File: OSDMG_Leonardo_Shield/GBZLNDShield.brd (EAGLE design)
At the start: 81.3 x 52.1 mm, 12 parts

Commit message: update
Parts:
- moved B1 31.5 mm to (67.5, 35.1)
- moved JP2 3.96 mm to (32.0, 45.4)
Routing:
- net N$8: track 79.8 -> 47.9 mm, vias 0 -> 3
- net N$10: track 15.0 -> 41.2 mm, vias 0 -> 1
- net N$7: track 47.7 -> 66.6 mm
- net N$3: track 52.2 -> 70.9 mm
- net N$5: track 92.2 -> 108.7 mm, vias 0 -> 1
- net N$12: track 53.7 -> 38.4 mm, vias 0 -> 1
- net N$1: track 62.6 -> 75.8 mm, vias 0 -> 2
- net N$14: track 21.3 -> 31.9 mm, vias 1 -> 2
- net N$2: track 65.6 -> 75.7 mm
- net N$11: track 69.8 -> 79.0 mm, vias 0 -> 2
- net N$6: track 15.6 -> 23.6 mm
- net N$4: track 52.1 -> 57.5 mm, vias 0 -> 1
- net N$15: track 25.3 -> 30.0 mm, vias 0 -> 1
- net N$13: track 50.4 -> 45.9 mm, vias 0 -> 1
- net N$9: track 21.7 -> 20.0 mm
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
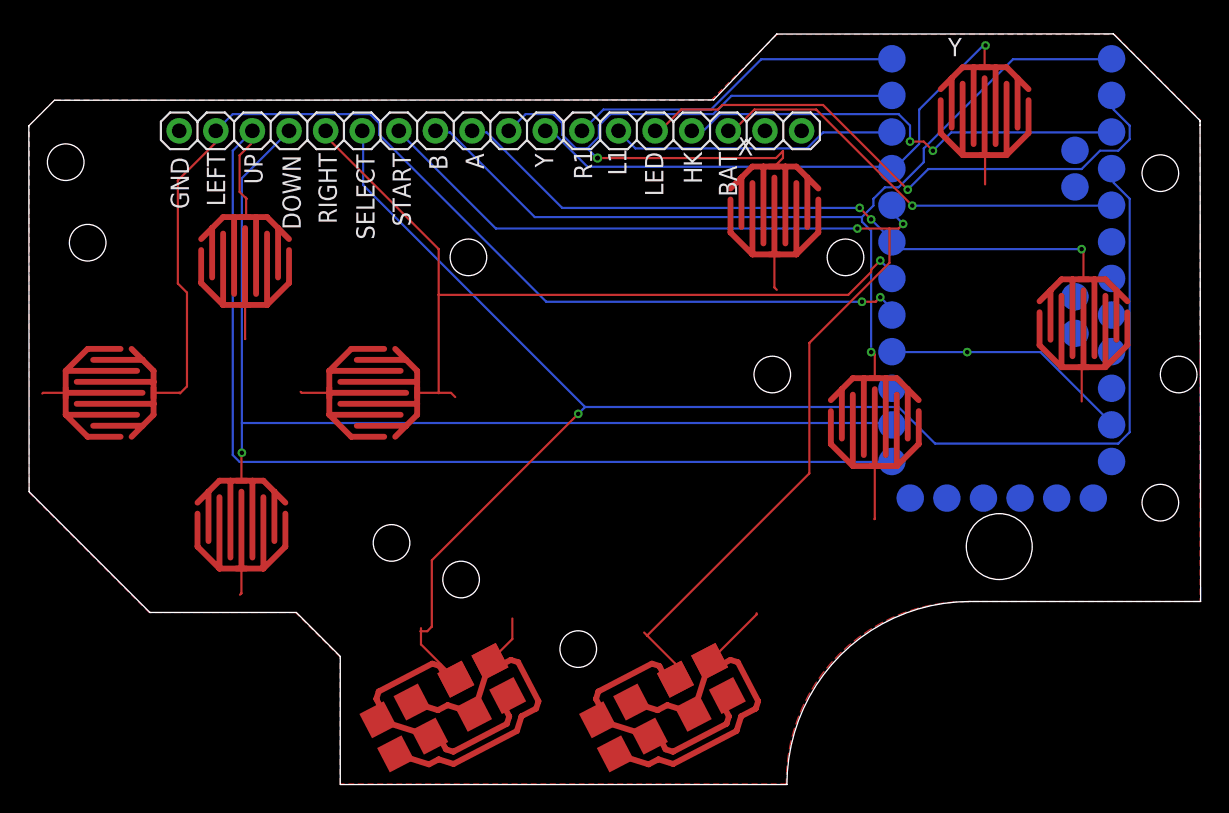
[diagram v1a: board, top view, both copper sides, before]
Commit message: update board
5V and GND Pads and better placement of the leonardo
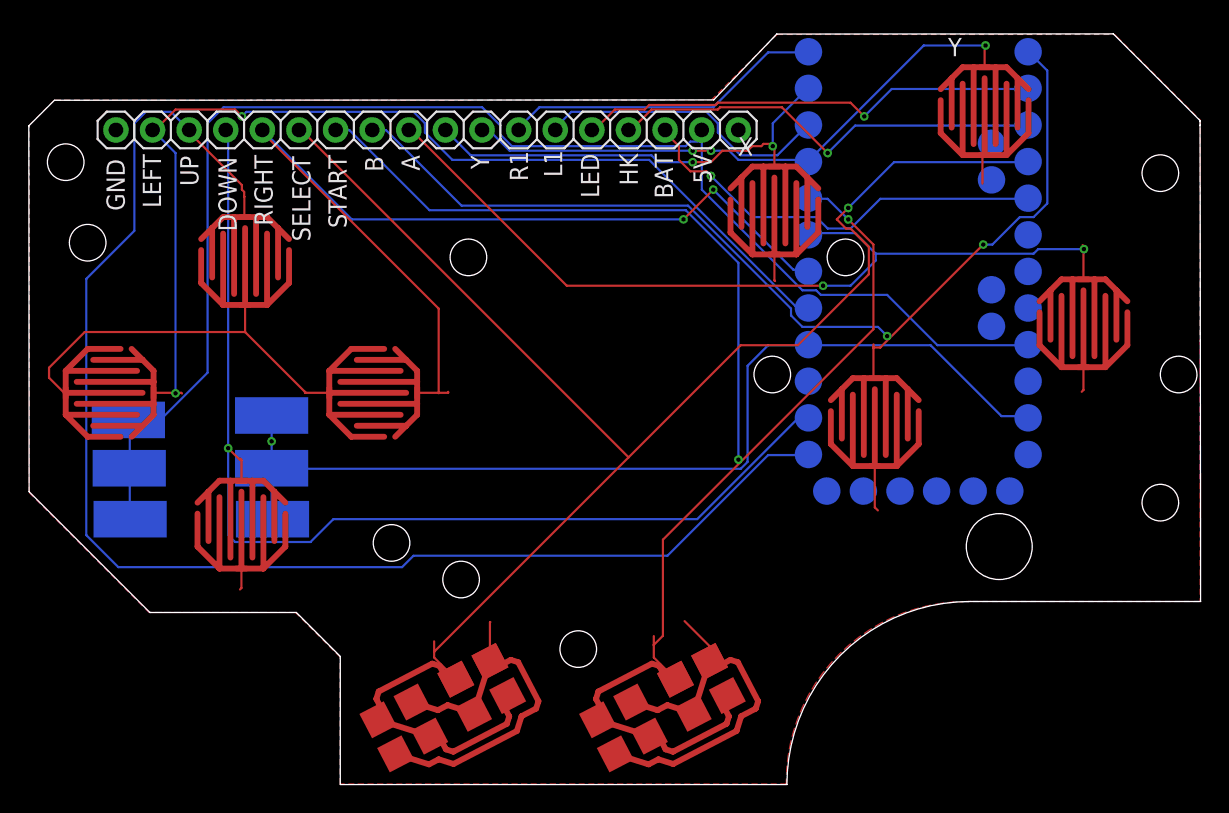
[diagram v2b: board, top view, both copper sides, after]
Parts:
- added PAD1, PAD2, PAD3, PAD4, PAD5, PAD6: (no value), wirepad:SMD2,54-5,08
- moved B1 5.81 mm to (61.7, 35.6)
- moved JP2 4.39 mm to (27.6, 45.4)
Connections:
- removed net VCC: B1.21
- new net N$17: B1.21, JP2.17, PAD1.1, PAD2.1, PAD3.1
- net GND: now also PAD4.1, PAD5.1, PAD6.1
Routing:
- net N$17: track 0.00 -> 99.6 mm
- net GND: track 44.3 -> 112.4 mm
- net N$2: track 75.7 -> 96.7 mm
- net N$13: track 45.9 -> 30.9 mm, vias 1 -> 2
- net N$8: track 47.9 -> 60.4 mm, vias 3 -> 2
- net N$5: track 108.7 -> 96.4 mm
- net N$4: track 57.5 -> 69.4 mm, vias 1 -> 2
- net N$11: track 79.0 -> 89.2 mm
- net N$10: track 41.2 -> 32.3 mm
- net N$7: track 66.6 -> 71.8 mm, vias 1 -> 2
- net N$3: track 70.9 -> 75.0 mm
- net N$12: track 38.4 -> 40.7 mm, vias 1 -> 3
- net N$1: track 75.8 -> 73.5 mm
- net N$14: track 31.9 -> 30.6 mm, vias 2 -> 1
- net N$6: track 23.6 -> 22.4 mm
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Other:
- board text added: "5V"
